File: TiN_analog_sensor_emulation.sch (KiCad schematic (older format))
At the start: 0 parts

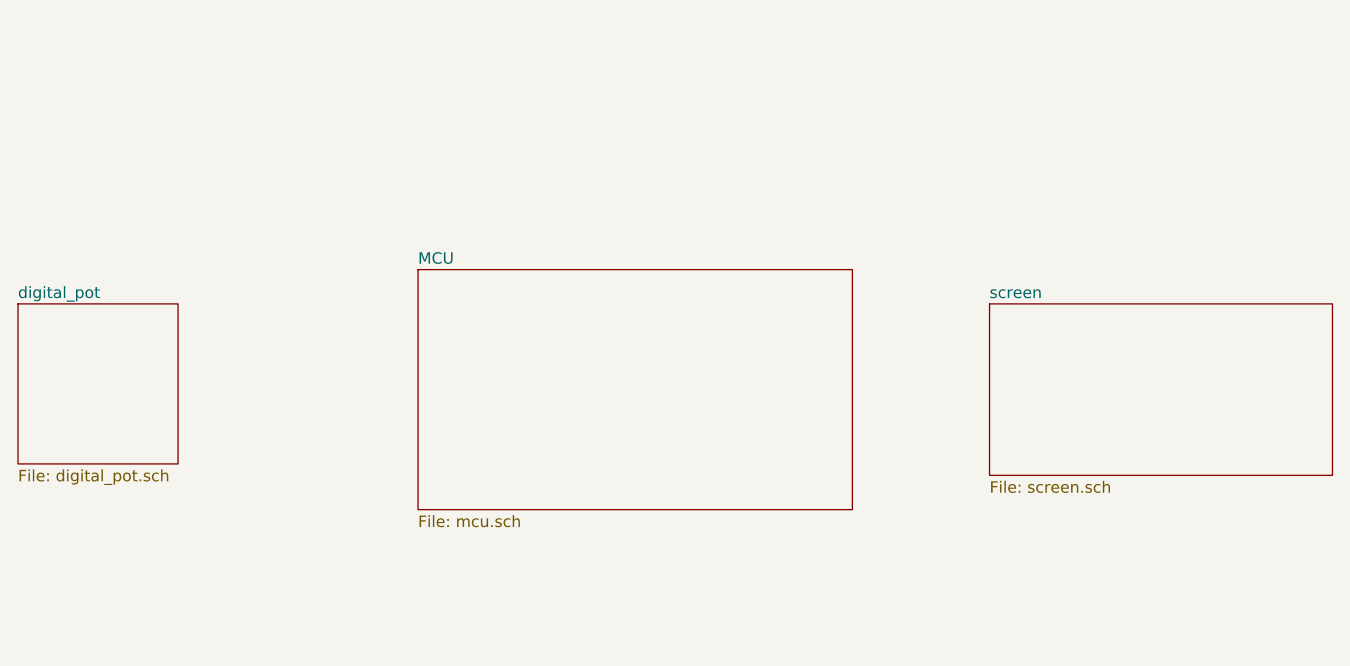
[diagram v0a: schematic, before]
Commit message: Praca nad sch, dodana sekcja zasilania i karta sd
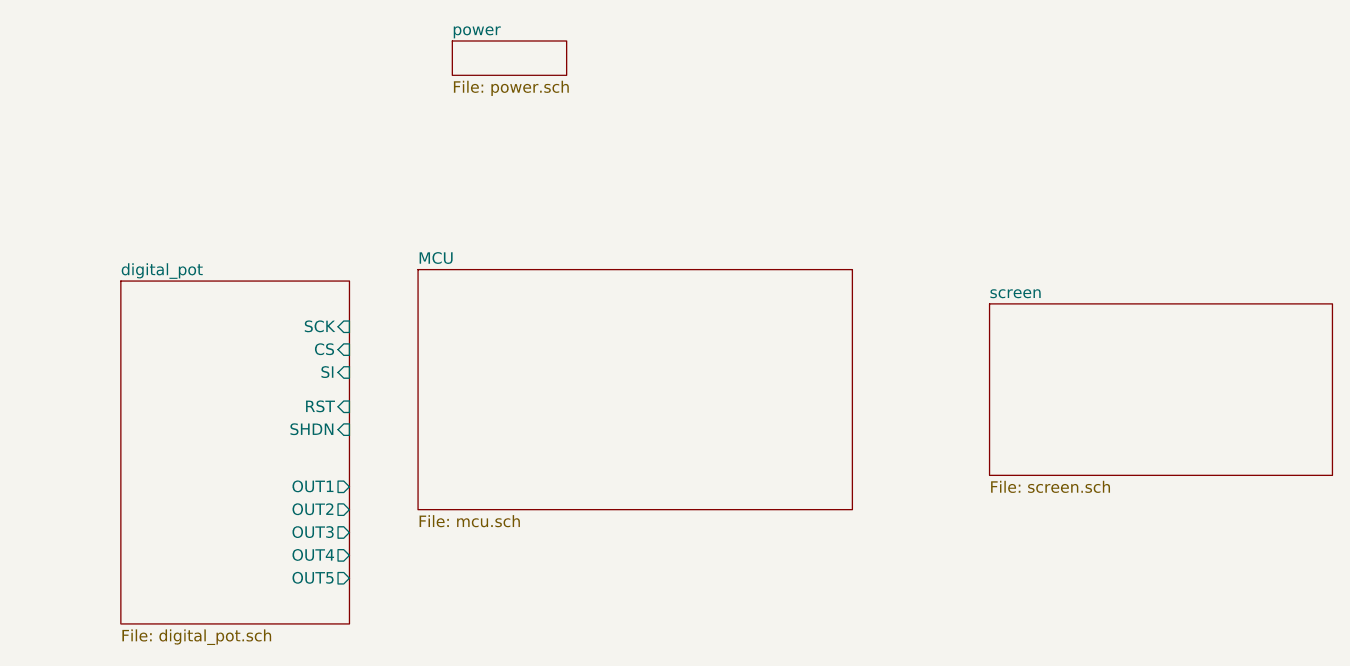
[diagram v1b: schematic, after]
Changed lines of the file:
@@
 EESchema Schematic File Version 4
+LIBS:TiN_analog_sensor_emulation-cache
 EELAYER 29 0
 EELAYER END
 $Descr A4 11693 8268
 encoding utf-8
-Sheet 1 4
+Sheet 1 5
 Title ""
 Date ""
@@
 $EndSheet
 $Sheet
-S 2550 2900 700  700
+S 3000 2800 1000 1500
 U 5CDEABB2
 F0 "digital_pot" 50
 F1 "digital_pot.sch" 50
+F2 "SCK" I R 4000 3000 50
+F3 "CS" I R 4000 3100 50
+F4 "SI" I R 4000 3200 50
+F5 "RST" I R 4000 3350 50
+F6 "SHDN" I R 4000 3450 50
+F7 "OUT1" O R 4000 3700 50
+F8 "OUT2" O R 4000 3800 50
+F9 "OUT3" O R 4000 3900 50
+F10 "OUT5" O R 4000 4100 50
+F11 "OUT4" O R 4000 4000 50
 $EndSheet
 $Sheet
@@
 F1 "screen.sch" 50
 $EndSheet
+$Sheet
+S 4450 1750 500  150
+U 5CDEEC5A
+F0 "power" 50
+F1 "power.sch" 50
+$EndSheet
 $EndSCHEMATC

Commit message: dalsza praca nad sch, przypisanie pinów
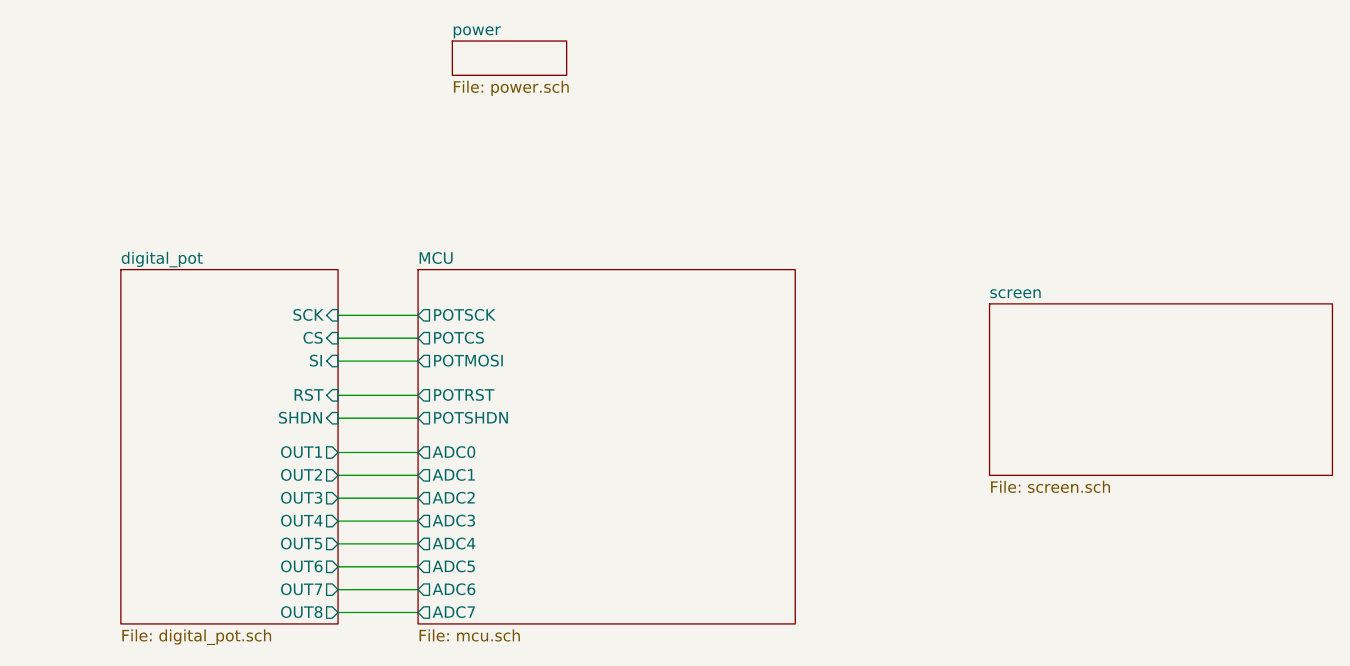
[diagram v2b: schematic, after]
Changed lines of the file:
@@
 $EndDescr
 $Sheet
-S 4300 2750 1900 1050
+S 4300 2750 1650 1550
 U 5CDEAB6D
 F0 "MCU" 50
 F1 "mcu.sch" 50
+F2 "POTSCK" O L 4300 2950 50
+F3 "POTMOSI" O L 4300 3150 50
+F4 "POTCS" O L 4300 3050 50
+F5 "ADC0" O L 4300 3550 50
+F6 "ADC1" O L 4300 3650 50
+F7 "ADC2" O L 4300 3750 50
+F8 "ADC3" O L 4300 3850 50
+F9 "ADC4" O L 4300 3950 50
+F10 "ADC5" O L 4300 4050 50
+F11 "ADC7" O L 4300 4250 50
+F12 "ADC6" O L 4300 4150 50
+F13 "POTRST" O L 4300 3300 50
+F14 "POTSHDN" O L 4300 3400 50
 $EndSheet
 $Sheet
-S 3000 2800 1000 1500
+S 3000 2750 950  1550
 U 5CDEABB2
 F0 "digital_pot" 50
 F1 "digital_pot.sch" 50
-F2 "SCK" I R 4000 3000 50
-F3 "CS" I R 4000 3100 50
-F4 "SI" I R 4000 3200 50
-F5 "RST" I R 4000 3350 50
-F6 "SHDN" I R 4000 3450 50
-F7 "OUT1" O R 4000 3700 50
-F8 "OUT2" O R 4000 3800 50
-F9 "OUT3" O R 4000 3900 50
-F10 "OUT5" O R 4000 4100 50
-F11 "OUT4" O R 4000 4000 50
+F2 "SCK" I R 3950 2950 50
+F3 "CS" I R 3950 3050 50
+F4 "SI" I R 3950 3150 50
+F5 "RST" I R 3950 3300 50
+F6 "SHDN" I R 3950 3400 50
+F7 "OUT1" O R 3950 3550 50
+F8 "OUT2" O R 3950 3650 50
+F9 "OUT3" O R 3950 3750 50
+F10 "OUT5" O R 3950 3950 50
+F11 "OUT4" O R 3950 3850 50
+F12 "OUT6" O R 3950 4050 50
+F13 "OUT7" O R 3950 4150 50
+F14 "OUT8" O R 3950 4250 50
 $EndSheet
 $Sheet
@@
 F1 "power.sch" 50
 $EndSheet
+Wire Wire Line
+	3950 4250 4300 4250
+Wire Wire Line
+	3950 4150 4300 4150
+Wire Wire Line
+	4300 4050 3950 4050
+Wire Wire Line
+	3950 3950 4300 3950
+Wire Wire Line
+	4300 3850 3950 3850
+Wire Wire Line
+	3950 3750 4300 3750
+Wire Wire Line
+	4300 3650 3950 3650
+Wire Wire Line
+	3950 3550 4300 3550
+Wire Wire Line
+	3950 2950 4300 2950
+Wire Wire Line
+	3950 3050 4300 3050
+Wire Wire Line
+	3950 3150 4300 3150
+Wire Wire Line
+	3950 3300 4300 3300
+Wire Wire Line
+	4300 3400 3950 3400
 $EndSCHEMATC
